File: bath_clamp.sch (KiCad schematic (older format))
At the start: 20 parts, among them U10 LP2951_SOIC, U6 24AA025UID, U7 LM337L_SO8, U9 MCP1804x-3302xOT

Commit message: updates to schematic for alternate part #s
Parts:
- removed U7: LM337L_SO8, Package_SO:SOIC-8_3.9x4.9mm_P1.27mm, symbol Regulator_Linear:LM337L_SO8
- added C19: 0.01u, Capacitor_SMD:C_0603_1608Metric, symbol Device:C
- added R66: 1, Resistor_SMD:R_0603_1608Metric, symbol Device:R_US
- added U7: MIC5270, agg:SOT-23-5, symbol agg-kicad:MIC5270
- C2: value 0.1u -> 1u; Manf# CC0603MRX7R8BB104 -> 06033C105KAT4A; Tolerance 20% -> 10%
- C3: value 1u -> 10u; footprint Capacitor_SMD:C_0603_1608Metric -> Capacitor_SMD:C_0805_2012Metric; Manf# CC0603MRX5R8BB105 -> (none)
- C5: value 0.1u -> 4.7u; Manf# CC0603MRX7R8BB104 -> CL10A475KP8NNNC
- R15: value 240 -> 487; Manf# RC0603FR-07240RL -> RC0603FR-07487RL
- R16: value 240 -> 1.13k; Manf# RC0603FR-07240RL -> RC0603FR-071K13L
- R17: value 1.13k -> 240; Manf# RC0603FR-071K13L -> RC0603FR-07240RL
- R51: Manf# (none) -> RC0603FR-070RL
- U10: Alternate Manf# (none) -> LP2951-03YM-TR
- U6: Alternate Manf# (none) -> 24AA025E64-I/SN
- U9: value MCP1804x-3302xOT -> LP2981A-33DBVT; symbol Regulator_Linear:MCP1804x-3302xOT -> Regulator_Linear:LP2985-3.3; Alternate Manf# (none) -> LP2985-33DBVR; Alternate2 Manf# (none) -> LP2985-33DBVRG4; Alternate3 Manf# (none) -> TPS7A2433DBVR; Manf# MCP1804T-3302I/OT -> LP2981A-33DBVT
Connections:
- wire segments 77 -> 80
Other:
- note added: "-Vout = -1.20*(1+rtop/240)\nAllow for fixed regulator (MIC5270-4.1YM5-TR): -4.1 V out \nor adjustable regulator (MIC5270YM5-TR)"
- note added: "ESR must be increased \nfor the LP2981\n(but not the LP2985)"
- note added: "Install 0.01u for the LP2985 to pin 4\nBut do NOT install for the LP2981"
- note removed: "-Vout = - 1.25*(1+r2/240)"
- moved on the sheet: C2, C3, C5, R14, R15

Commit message: nearly completed layout re-route
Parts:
- U7: footprint agg:SOT-23-5 -> Package_TO_SOT_SMD:TSOT-23-5
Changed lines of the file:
@@
 F 0 "U7" H 2800 3225 50  0000 C CNN
 F 1 "MIC5270" H 2800 3134 50  0000 C CNN
-F 2 "agg:SOT-23-5" H 2500 2600 50  0001 L CNN
+F 2 "Package_TO_SOT_SMD:TSOT-23-5" H 2500 2600 50  0001 L CNN
 F 3 "http://ww1.microchip.com/downloads/en/DeviceDoc/mic5270.pdf" H 2500 2500 50  0001 L CNN
 F 4 "2510308" H 2500 2400 50  0001 L CNN "Farnell"

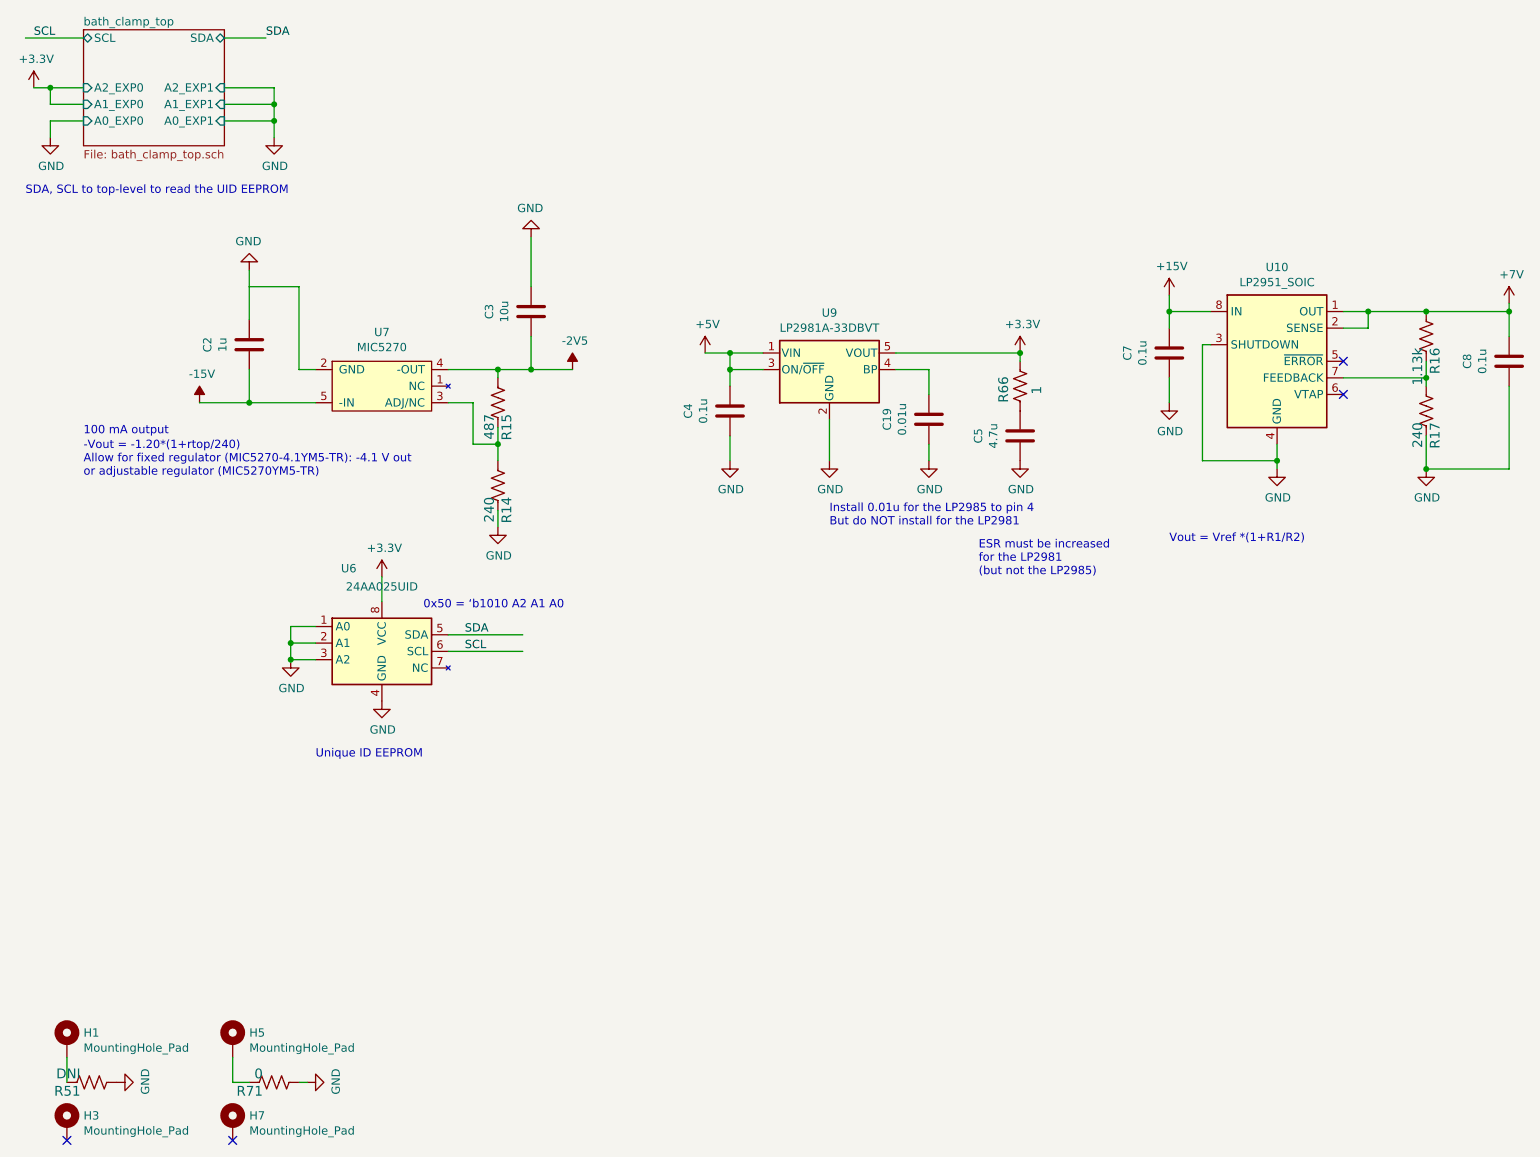
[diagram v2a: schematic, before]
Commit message: gerbers, BOM and fabrication files sent to PCBway
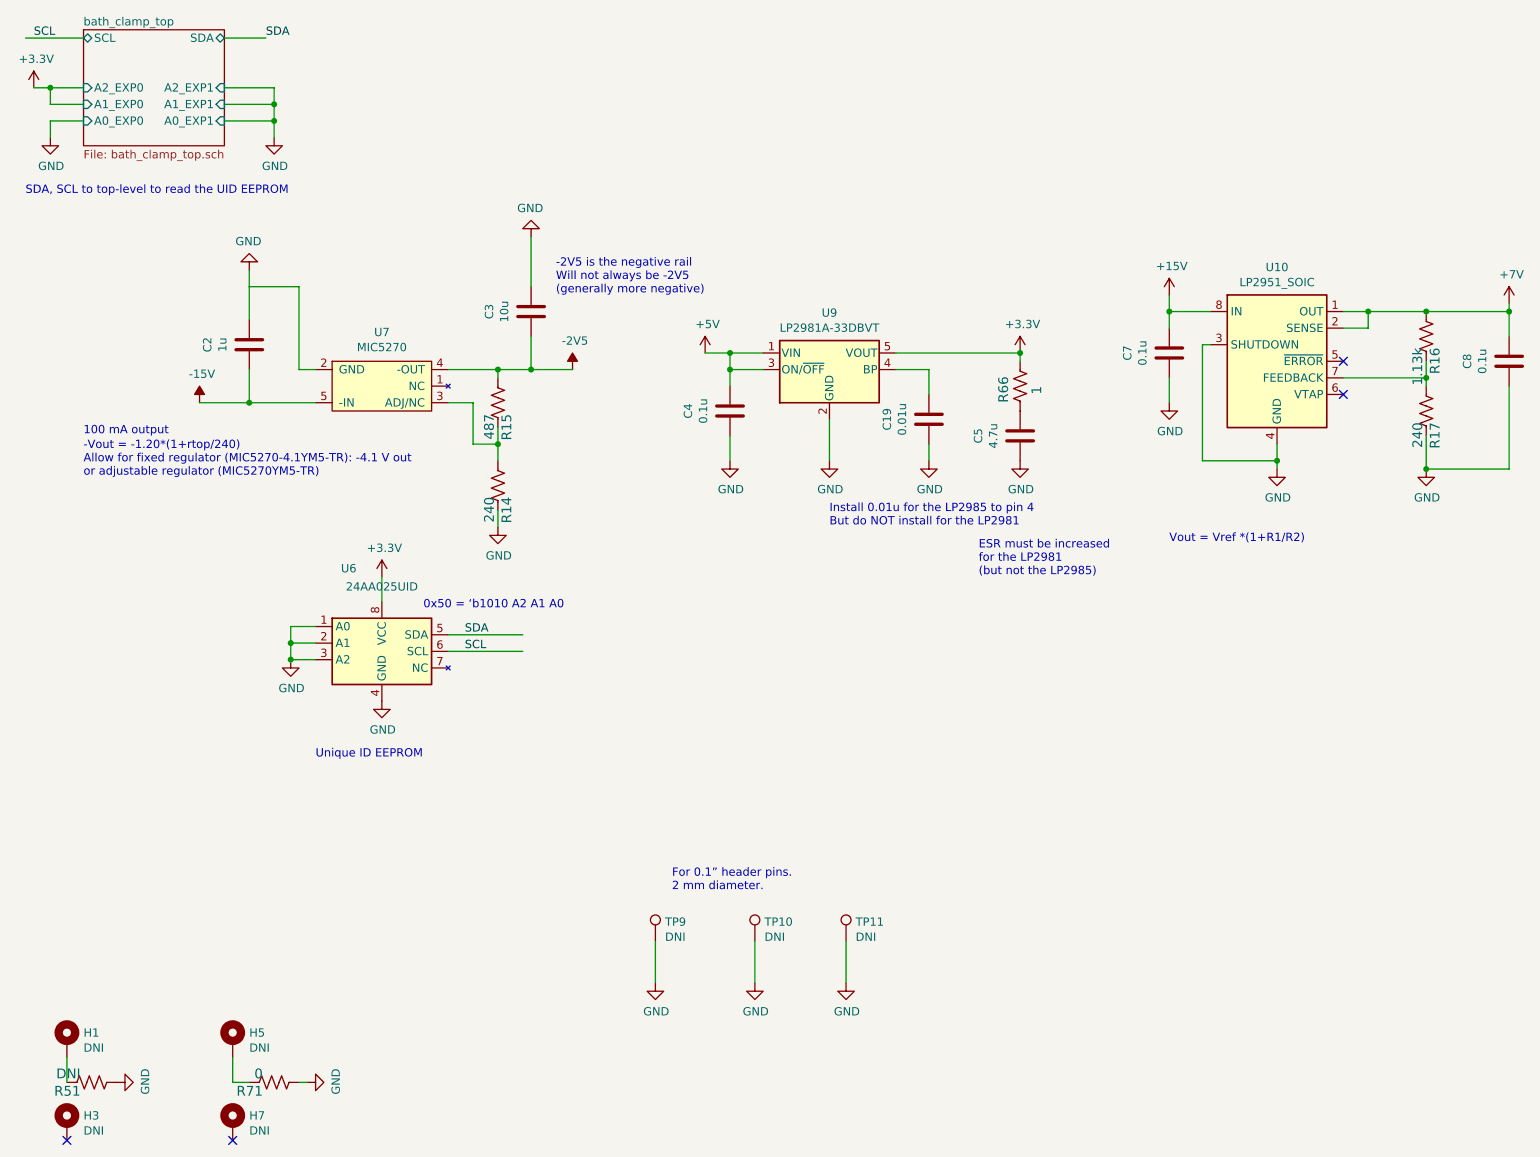
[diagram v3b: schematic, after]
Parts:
- added TP10, TP11, TP9: DNI, TestPoint:TestPoint_THTPad_D2.0mm_Drill1.0mm, symbol Connector:TestPoint
- C3: Manf# (none) -> CL21A106KOQNNNE; Tolerance 20% -> 10%; voltage 25V -> 16V
- H1, H3, H5, H7: value MountingHole_Pad -> DNI
- U10: Alternate2 Manf# (none) -> LP2951ACDR2G; Manf# LP2951ACDR2G -> LP2951-30DR
- U7: Farnell 2510308 -> (none); Notes (none) -> TSOT vs SOT is just the height
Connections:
- wire segments 80 -> 83
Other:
- note added: "-2V5 is the negative rail\nWill not always be -2V5\n(generally more negative)"
- note added: "For 0.1” header pins. \n2 mm diameter."
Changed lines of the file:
@@
 F 2 "Capacitor_SMD:C_0805_2012Metric" H 3738 2300 50  0001 C CNN
 F 3 "~" H 3700 2450 50  0001 C CNN
-F 4 "" H 3448 2550 50  0001 C CNN "Manf#"
-F 5 "20%" H 3448 2550 50  0001 C CNN "Tolerance"
-F 6 "25V" H 3448 2550 50  0001 C CNN "voltage"
+F 4 "CL21A106KOQNNNE" H 3448 2550 50  0001 C CNN "Manf#"
+F 5 "10%" H 3448 2550 50  0001 C CNN "Tolerance"
+F 6 "16V" H 3448 2550 50  0001 C CNN "voltage"
 	1    3700 2450
 	1    0    0    -1
@@
 F 2 "Package_SO:SOIC-8_3.9x4.9mm_P1.27mm" H 8200 2100 50  0001 C CNN
 F 3 "http://www.ti.com/lit/ds/symlink/lp2951-n.pdf" H 8200 2750 50  0001 C CNN
-F 4 "LP2951ACDR2G" H 8200 3417 50  0001 C CNN "Manf#"
+F 4 "LP2951-30DR" H 8200 3417 50  0001 C CNN "Manf#"
 F 5 "LP2951-03YM-TR" H 8200 2750 50  0001 C CNN "Alternate Manf#"
+F 6 "LP2951ACDR2G" H 8200 2750 50  0001 C CNN "Alternate2 Manf#"
 	1    8200 2750
 	1    0    0    -1
@@
 AR Path="/60EC1EFA" Ref="H1"  Part="1"
 F 0 "H1" H 1000 6899 50  0000 L CNN
-F 1 "MountingHole_Pad" H 1000 6808 50  0000 L CNN
+F 1 "DNI" H 1000 6808 50  0000 L CNN
 F 2 "MountingHole:MountingHole_3.2mm_M3_DIN965_Pad" H 900 6850 50  0001 C CNN
 F 3 "~" H 900 6850 50  0001 C CNN
@@
 AR Path="/60EC1F00" Ref="H3"  Part="1"
 F 0 "H3" H 1000 7399 50  0000 L CNN
-F 1 "MountingHole_Pad" H 1000 7308 50  0000 L CNN
+F 1 "DNI" H 1000 7308 50  0000 L CNN
 F 2 "MountingHole:MountingHole_3.2mm_M3_DIN965_Pad" H 900 7350 50  0001 C CNN
 F 3 "~" H 900 7350 50  0001 C CNN
@@
 AR Path="/60EC1F06" Ref="H7"  Part="1"
 F 0 "H7" H 2000 7399 50  0000 L CNN
-F 1 "MountingHole_Pad" H 2000 7308 50  0000 L CNN
+F 1 "DNI" H 2000 7308 50  0000 L CNN
 F 2 "MountingHole:MountingHole_3.2mm_M3_DIN965_Pad" H 1900 7350 50  0001 C CNN
 F 3 "~" H 1900 7350 50  0001 C CNN
@@
 AR Path="/60EC1F0C" Ref="H5"  Part="1"
 F 0 "H5" H 2000 6899 50  0000 L CNN
-F 1 "MountingHole_Pad" H 2000 6808 50  0000 L CNN
+F 1 "DNI" H 2000 6808 50  0000 L CNN
 F 2 "MountingHole:MountingHole_3.2mm_M3_DIN965_Pad" H 1900 6850 50  0001 C CNN
 F 3 "~" H 1900 6850 50  0001 C CNN
@@
 F 2 "Package_TO_SOT_SMD:TSOT-23-5" H 2500 2600 50  0001 L CNN
 F 3 "http://ww1.microchip.com/downloads/en/DeviceDoc/mic5270.pdf" H 2500 2500 50  0001 L CNN
-F 4 "2510308" H 2500 2400 50  0001 L CNN "Farnell"
-F 5 "MIC5270-4.1YM5-TR" H 2800 2900 50  0001 C CNN "Manf#"
-F 6 "MIC5270YM5-TR" H 2800 2900 50  0001 C CNN "Alternate Manf#"
+F 4 "MIC5270-4.1YM5-TR" H 2800 2900 50  0001 C CNN "Manf#"
+F 5 "MIC5270YM5-TR" H 2800 2900 50  0001 C CNN "Alternate Manf#"
+F 6 "TSOT vs SOT is just the height" H 2800 2900 50  0001 C CNN "Notes"
 	1    2800 2900
 	1    0    0    -1
@@
 	5900 2700 6650 2700
 Connection ~ 6650 2700
+Wire Wire Line
+	4450 6250 4450 6500
+$Comp
+L Connector:TestPoint TP10
+U 1 1 62528920
+P 5050 6250
+F 0 "TP10" H 5108 6368 50  0000 L CNN
+F 1 "DNI" H 5108 6277 50  0000 L CNN
+F 2 "TestPoint:TestPoint_THTPad_D2.0mm_Drill1.0mm" H 5250 6250 50  0001 C CNN
+F 3 "~" H 5250 6250 50  0001 C CNN
+	1    5050 6250
+	1    0    0    -1
+$EndComp
+Wire Wire Line
+	5050 6250 5050 6500
+$Comp
+L power:GND #PWR0216
+U 1 1 6252892B
+P 5050 6500
+F 0 "#PWR0216" H 5050 6250 50  0001 C CNN
+F 1 "GND" H 5055 6327 50  0000 C CNN
+F 2 "" H 5050 6500 50  0001 C CNN
+F 3 "" H 5050 6500 50  0001 C CNN
+	1    5050 6500
+	1    0    0    -1
+$EndComp
+$Comp
+L Connector:TestPoint TP11
+U 1 1 62528935
+P 5600 6250
+F 0 "TP11" H 5658 6368 50  0000 L CNN
+F 1 "DNI" H 5658 6277 50  0000 L CNN
+F 2 "TestPoint:TestPoint_THTPad_D2.0mm_Drill1.0mm" H 5800 6250 50  0001 C CNN
+F 3 "~" H 5800 6250 50  0001 C CNN
+	1    5600 6250
+	1    0    0    -1
+$EndComp
+Wire Wire Line
+	5600 6250 5600 6500
+$Comp
+L power:GND #PWR0217
+U 1 1 62528940
+P 5600 6500
+F 0 "#PWR0217" H 5600 6250 50  0001 C CNN
+F 1 "GND" H 5605 6327 50  0000 C CNN
+F 2 "" H 5600 6500 50  0001 C CNN
+F 3 "" H 5600 6500 50  0001 C CNN
+	1    5600 6500
+	1    0    0    -1
+$EndComp
+$Comp
+L Connector:TestPoint TP9
+U 1 1 625BD5CD
+P 4450 6250
+F 0 "TP9" H 4508 6368 50  0000 L CNN
+F 1 "DNI" H 4508 6277 50  0000 L CNN
+F 2 "TestPoint:TestPoint_THTPad_D2.0mm_Drill1.0mm" H 4650 6250 50  0001 C CNN
+F 3 "~" H 4650 6250 50  0001 C CNN
+	1    4450 6250
+	1    0    0    -1
+$EndComp
+$Comp
+L power:GND #PWR0218
+U 1 1 625BD5D8
+P 4450 6500
+F 0 "#PWR0218" H 4450 6250 50  0001 C CNN
+F 1 "GND" H 4455 6327 50  0000 C CNN
+F 2 "" H 4450 6500 50  0001 C CNN
+F 3 "" H 4450 6500 50  0001 C CNN
+	1    4450 6500
+	1    0    0    -1
+$EndComp
+Text Notes 4550 5950 0    50   ~ 0
+For 0.1” header pins. \n2 mm diameter.
+Text Notes 3850 2350 0    50   ~ 0
+-2V5 is the negative rail\nWill not always be -2V5\n(generally more negative)
 $EndSCHEMATC
